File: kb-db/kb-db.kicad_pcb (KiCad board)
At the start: 2 copper layers, 42 x 11 mm, 12 parts, among them J1 Conn_01x04

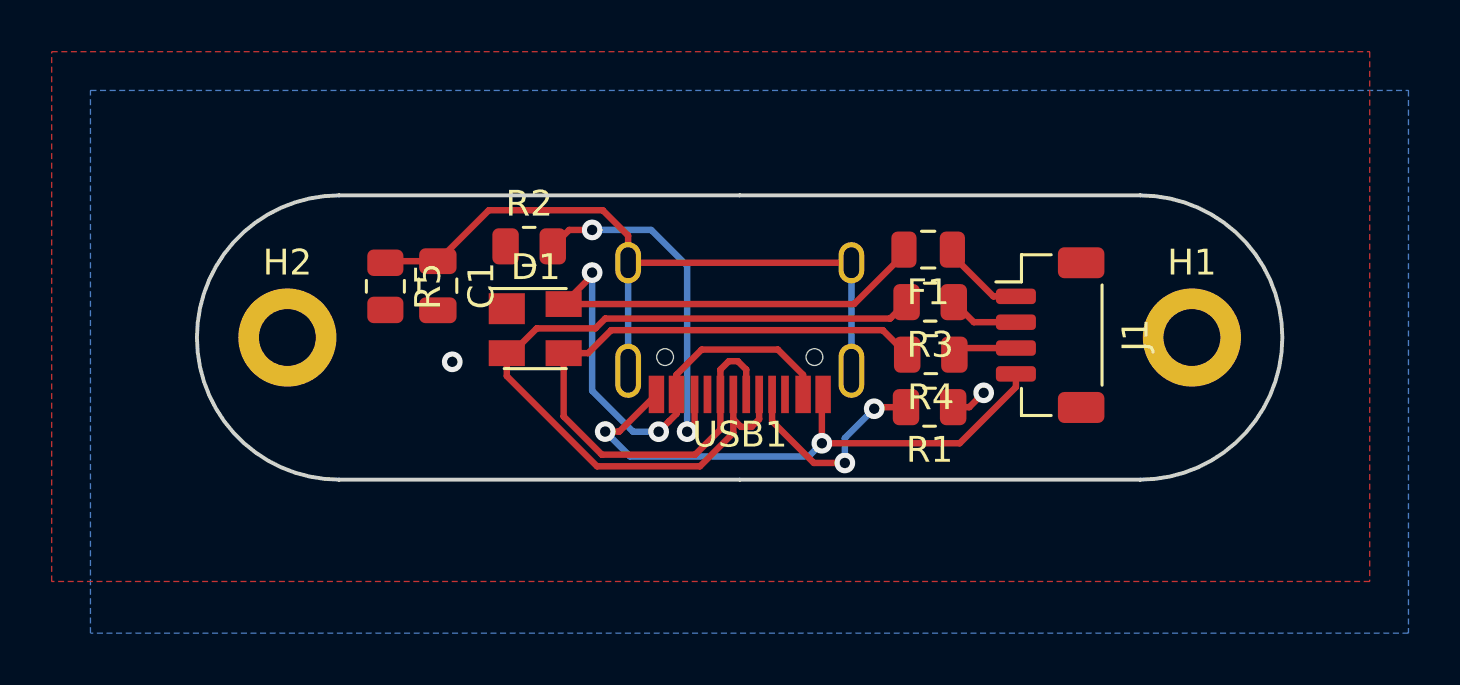
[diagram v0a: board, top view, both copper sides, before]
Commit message: Added production data
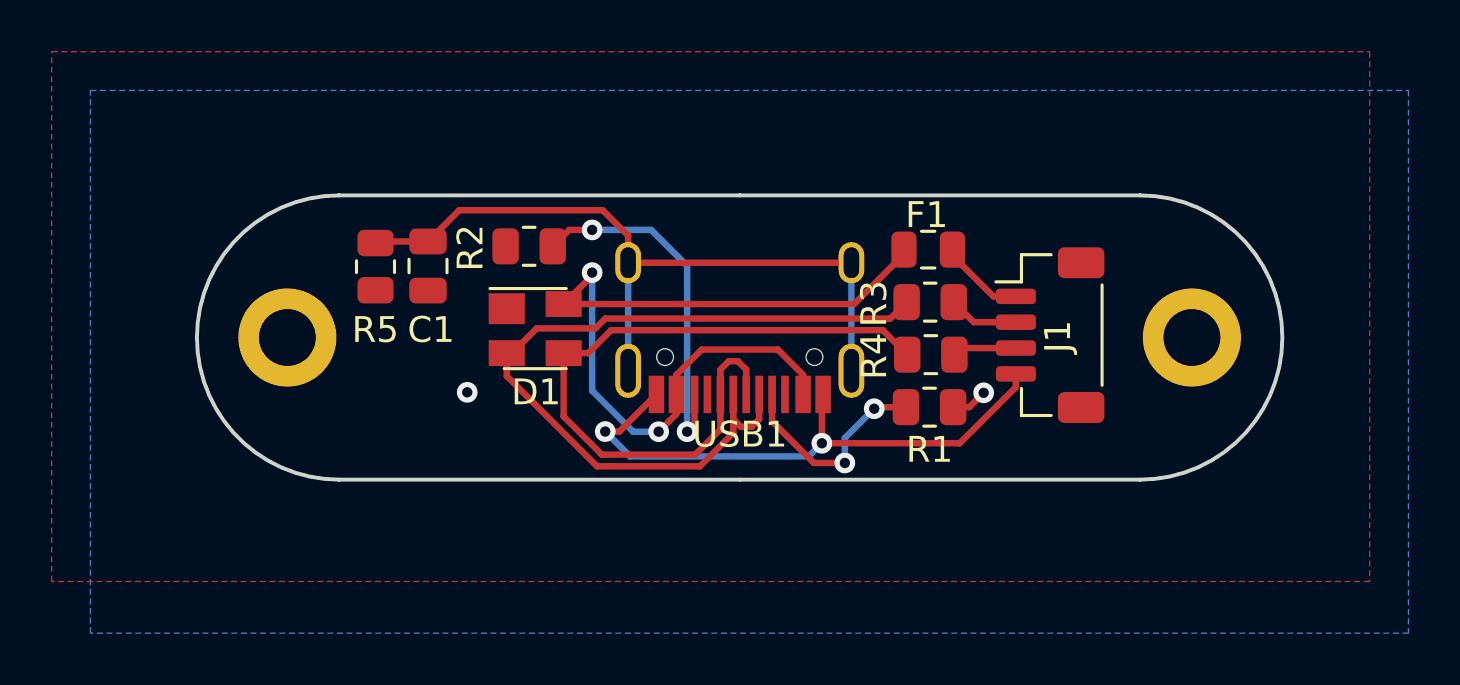
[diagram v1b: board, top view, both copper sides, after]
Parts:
- moved C1 0.85 mm to (66.9, 60.7)
- moved R5 0.85 mm to (64.9, 60.7)

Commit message: Ground components to USB ground
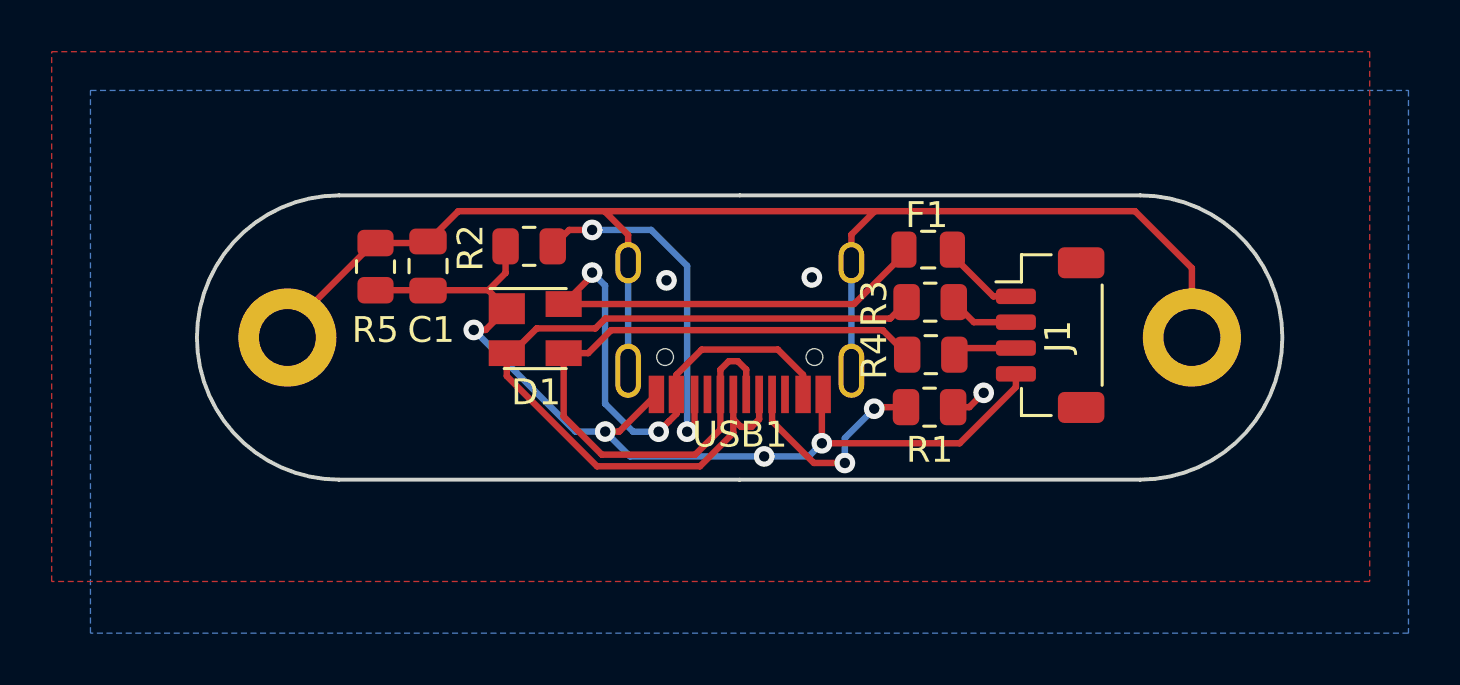
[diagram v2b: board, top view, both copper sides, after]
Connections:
- C1 pad 1: Net-(C1-Pad1) -> Earth
- C1 pad 2: Earth -> GND
- D1 pad 1: Earth -> GND
- R1 pad 1: Earth -> GND
- R2 pad 1: Earth -> GND
- R5 pad 1: Net-(C1-Pad1) -> Earth
- R5 pad 2: Earth -> GND
- USB1 pad 13: Net-(C1-Pad1) -> Earth
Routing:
- net Earth: track 1.41 -> 53.9 mm, vias 2 -> 0
- net Net-(C1-Pad1): track 28.8 -> 0.00 mm
- net GND: track 22.4 -> 39.5 mm, vias 2 -> 7
- added copper zone on B.Cu, net GND
- added copper zone on F.Cu, net GND
- removed copper zone on B.Cu, net Earth
- removed copper zone on F.Cu, net Earth
